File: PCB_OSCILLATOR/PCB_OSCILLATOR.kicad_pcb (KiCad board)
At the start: 2 copper layers, 96.8 x 43.9 mm, 96 parts, among them J1 Jumper, J10 Jumper, J11 Jumper, J12 Jumper, J13 Jumper, J14 Jumper, J15 Jumper, J16 Jumper, J2 Jumper, J3 Jumper, J4 Jumper, J5 Jumper, J6 Jumper, J7 Jumper, J8 Jumper, J9 Jumper, P1 CONN_01X04, P2 MCLK_EXTERNAL, P3 SPI_AD5270_1, P4 SPI_AD5270_2, P5 SPI_AD9833_1, P6 SPI_AD9833_2, P7 CONN_01X04, U1 AD5270, U10 ADR291, U2 AD8421, U3 AD9833, U4 AD5270, U5 AD8421, U6 AD9833, U7 ADG819, U8 ADP3303, U9 AD8651

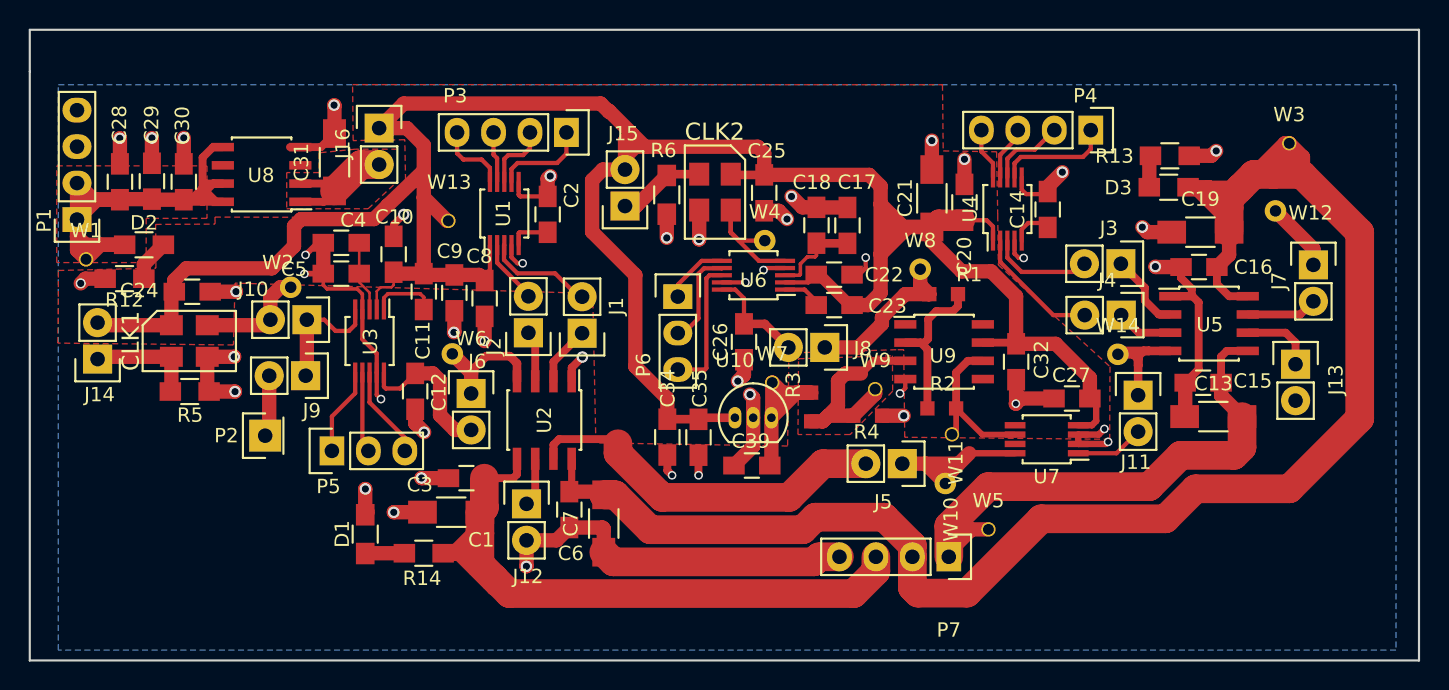
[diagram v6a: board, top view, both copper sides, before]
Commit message: PBC  99%
Faltan solo vias para conectar planos de tierras (Definir si se hace
plano de tierrta a la parte inferior izquierda//
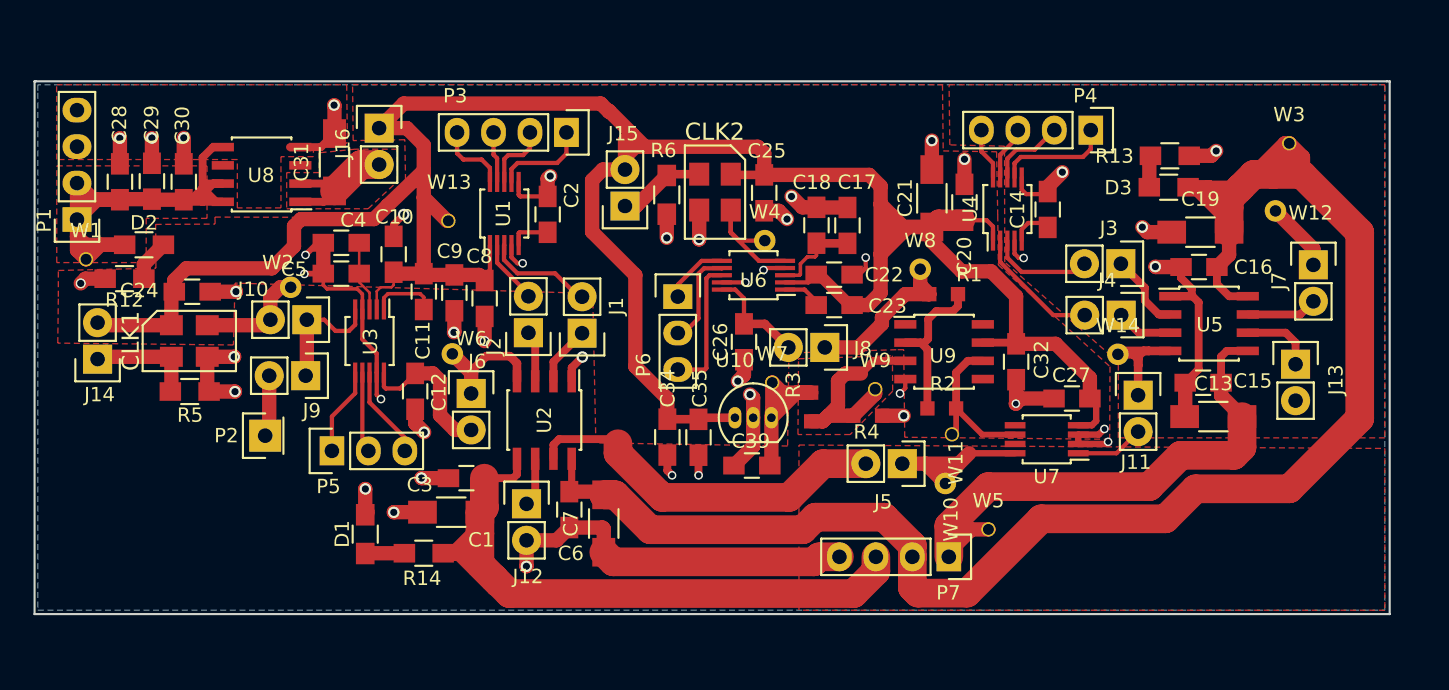
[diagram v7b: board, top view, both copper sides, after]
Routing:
- added copper zone on F.Cu, net /+12V
- added copper zone on F.Cu, net /GND
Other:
- board size 96.8 x 43.9 mm -> 94.4 x 37.1 mm
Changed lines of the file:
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@@
     (links 188)
     (no_connects 1)
-    (area 62.124999 62.284999 159.065001 106.375001)
+    (area 62.454999 65.874999 157.025001 103.145001)
     (thickness 1.6)
-    (drawings 5)
+    (drawings 6)
     (tracks 689)
     (zones 0)
@@
   )
   (setup
-    (last_trace_width 0.45)
+    (last_trace_width 0.2)
     (user_trace_width 0.3)
     (user_trace_width 0.35)
@@
     (visible_elements 7FFEFFFF)
     (pcbplotparams
-      (layerselection 0x00030_80000001)
+      (layerselection 0x3ffff_80000001)
       (usegerberextensions false)
       (excludeedgelayer true)
@@
       (drillshape 0)
       (scaleselection 1)
-      (outputdirectory ""))
+      (outputdirectory ../../../../Desktop/Paneles/))
   )
   (net 0 "")
@@
     (descr "Through hole socket strip")
     (tags "socket strip")
-    (fp_text reference P7 (at 0 -5.1 180) (layer F.SilkS)
+    (fp_text reference P7 (at 0.03 -2.51 180) (layer F.SilkS)
       (effects (font (size 1 1) (thickness 0.15)))
     )
@@
     )
   )
-  (gr_line (start 62.2 62.36) (end 62.2 65.28) (angle 90) (layer Edge.Cuts) (width 0.15))
-  (gr_line (start 158.99 62.36) (end 62.2 62.36) (angle 90) (layer Edge.Cuts) (width 0.15))
-  (gr_line (start 158.99 106.3) (end 158.99 62.36) (angle 90) (layer Edge.Cuts) (width 0.15))
-  (gr_line (start 62.2 106.3) (end 158.99 106.3) (angle 90) (layer Edge.Cuts) (width 0.15))
-  (gr_line (start 62.2 65.28) (end 62.2 106.3) (angle 90) (layer Edge.Cuts) (width 0.15))
+  (gr_line (start 62.53 65.95) (end 62.63 65.95) (angle 90) (layer Edge.Cuts) (width 0.15))
+  (gr_line (start 62.53 103.07) (end 62.53 65.95) (angle 90) (layer Edge.Cuts) (width 0.15))
+  (gr_line (start 156.95 103.07) (end 62.53 103.07) (angle 90) (layer Edge.Cuts) (width 0.15))
+  (gr_line (start 156.95 65.95) (end 156.95 103.07) (angle 90) (layer Edge.Cuts) (width 0.15))
+  (gr_line (start 156.75 65.95) (end 156.95 65.95) (angle 90) (layer Edge.Cuts) (width 0.15))
+  (gr_line (start 62.63 65.95) (end 156.75 65.95) (angle 90) (layer Edge.Cuts) (width 0.15))
   (segment (start 142.98 71.14) (end 144.52 71.14) (width 1) (layer F.Cu) (net 1))
   (via (at 144.86 70.8) (size 0.8) (drill 0.5) (layers F.Cu B.Cu) (net 1))
@@
     )
   )
-  (zone (net 1) (net_name /GND) (layer B.Cu) (hatch edge 0.508)
-    (connect_pads (clearance 0.3))
-    (min_thickness 0.2)
-    (fill yes (arc_segments 16) (thermal_gap 0.508) (thermal_bridge_width 0.508) (smoothing fillet))
-    (polygon
-      (pts
-        (xy 157.39 105.58) (xy 64.19 105.58) (xy 64.19 66.19) (xy 157.39 66.19) (xy 157.39 105.58)
-      )
-    )
-  )
   (zone (net 4) (net_name /VDD) (layer F.Cu) (hatch edge 0.508)
     (connect_pads (clearance 0.4))
@@
       )
     )
+  )
+  (zone (net 1) (net_name /GND) (layer B.Cu) (hatch edge 0.508)
+    (connect_pads (clearance 0.4))
+    (min_thickness 0.2)
+    (fill yes (arc_segments 16) (thermal_gap 0.508) (thermal_bridge_width 0.508) (smoothing fillet))
+    (polygon
+      (pts
+        (xy 62.76 66.75) (xy 62.76 102.8) (xy 156.61 102.8) (xy 156.61 66.19) (xy 62.76 66.19)
+        (xy 62.76 66.75)
+      )
+    )
+  )
+  (zone (net 1) (net_name /GND) (layer F.Cu) (hatch edge 0.508)
+    (connect_pads (clearance 0.4))
+    (min_thickness 0.2)
+    (fill yes (arc_segments 16) (thermal_gap 0.508) (thermal_bridge_width 0.508))
+    (polygon
+      (pts
+        (xy 84.33 70.21) (xy 84.14 70.33) (xy 81.96 70.51) (xy 81.96 71.2) (xy 79.7 71.2)
+        (xy 79.7 74.77) (xy 76.66 74.77) (xy 76.66 71.4) (xy 64.07 71.4) (xy 64.07 66.19)
+        (xy 84.28 66.19) (xy 84.33 70.21)
+      )
+    )
+  )
+  (zone (net 1) (net_name /GND) (layer F.Cu) (hatch edge 0.508)
+    (connect_pads (clearance 0.4))
+    (min_thickness 0.2)
+    (fill yes (arc_segments 16) (thermal_gap 0.508) (thermal_bridge_width 0.508))
+    (polygon
+      (pts
+        (xy 126.25 66.19) (xy 156.61 66.19) (xy 156.61 90.79) (xy 138.04 90.79) (xy 138.04 85.63)
+        (xy 138.04 85.52) (xy 130.13 78.55) (xy 130.11 70.57) (xy 130.11 70.47) (xy 126.3 70.38)
+        (xy 126.25 66.19)
+      )
+    )
+  )
+  (zone (net 46) (net_name /+12V) (layer F.Cu) (hatch edge 0.508)
+    (connect_pads (clearance 0.4))
+    (min_thickness 0.2)
+    (fill yes (arc_segments 16) (thermal_gap 0.508) (thermal_bridge_width 0.508))
+    (polygon
+      (pts
+        (xy 156.61 91.53) (xy 156.61 102.8) (xy 115.79 102.8) (xy 115.79 91.29) (xy 156.61 91.53)
+      )
+    )

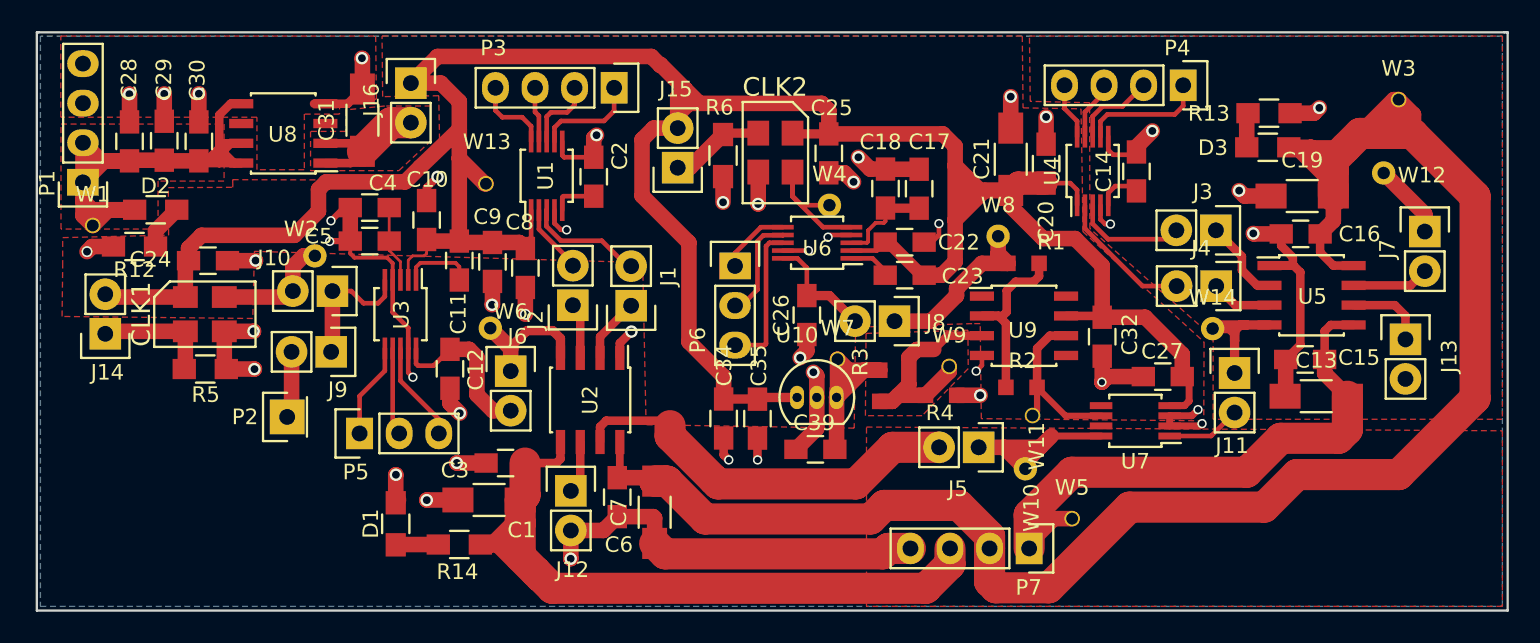
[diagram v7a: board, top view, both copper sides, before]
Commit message: PCB 100%
Planos terminados, vias faltantes agregadas, colocación de los nombres,
falta realizar una última revisión para tratar de identificar errores y
depurarlos.
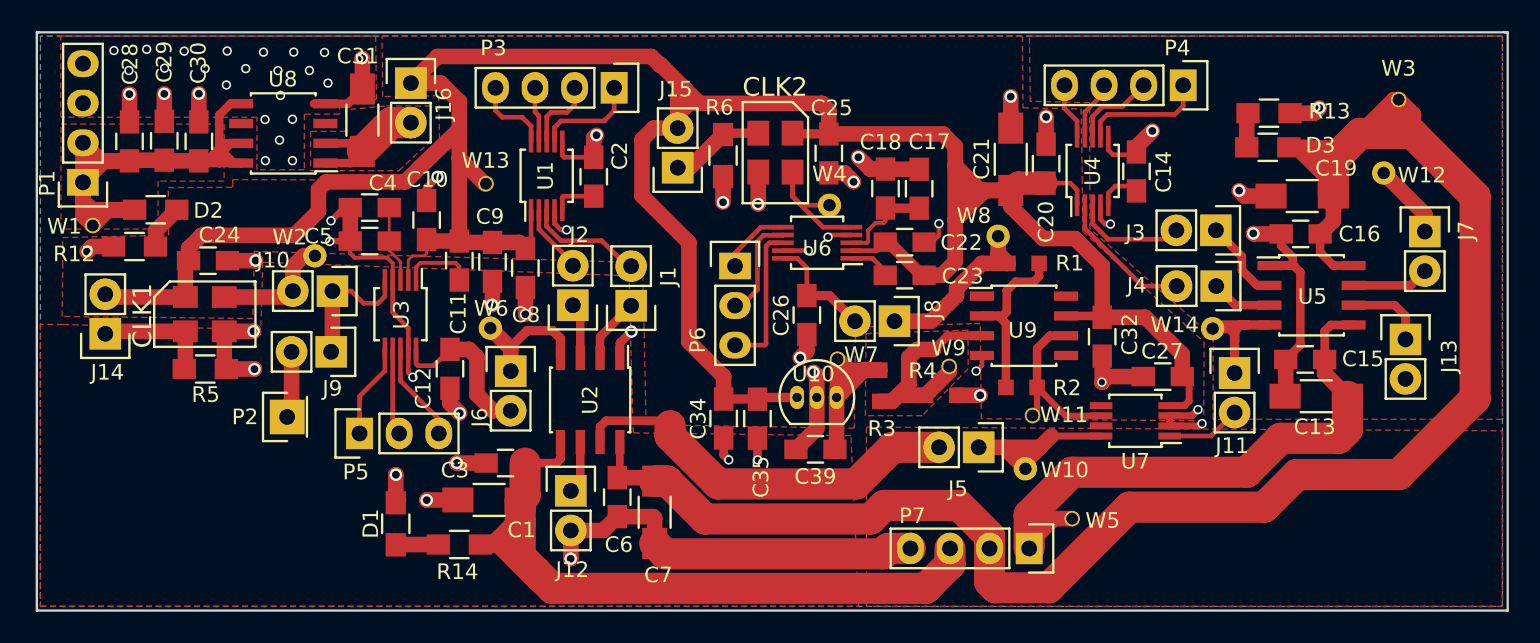
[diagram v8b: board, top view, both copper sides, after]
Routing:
- net /GND: vias 45 -> 66
- added copper zone on F.Cu, net (none)
